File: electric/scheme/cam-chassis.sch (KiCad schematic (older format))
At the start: 45 parts, among them IC1 ATMEGA8-AI, K1 pyro, P1 TST, P2 TST, P3 TST, P4 TST, P5 TST, P6 TST, P7 servo, Q3 bc857, Q4 bc847, Q5 irlml2244, Q6 NPN, Q7 irlml2244, U1 MINI-USB-B-4-bases, Y1 Crystal

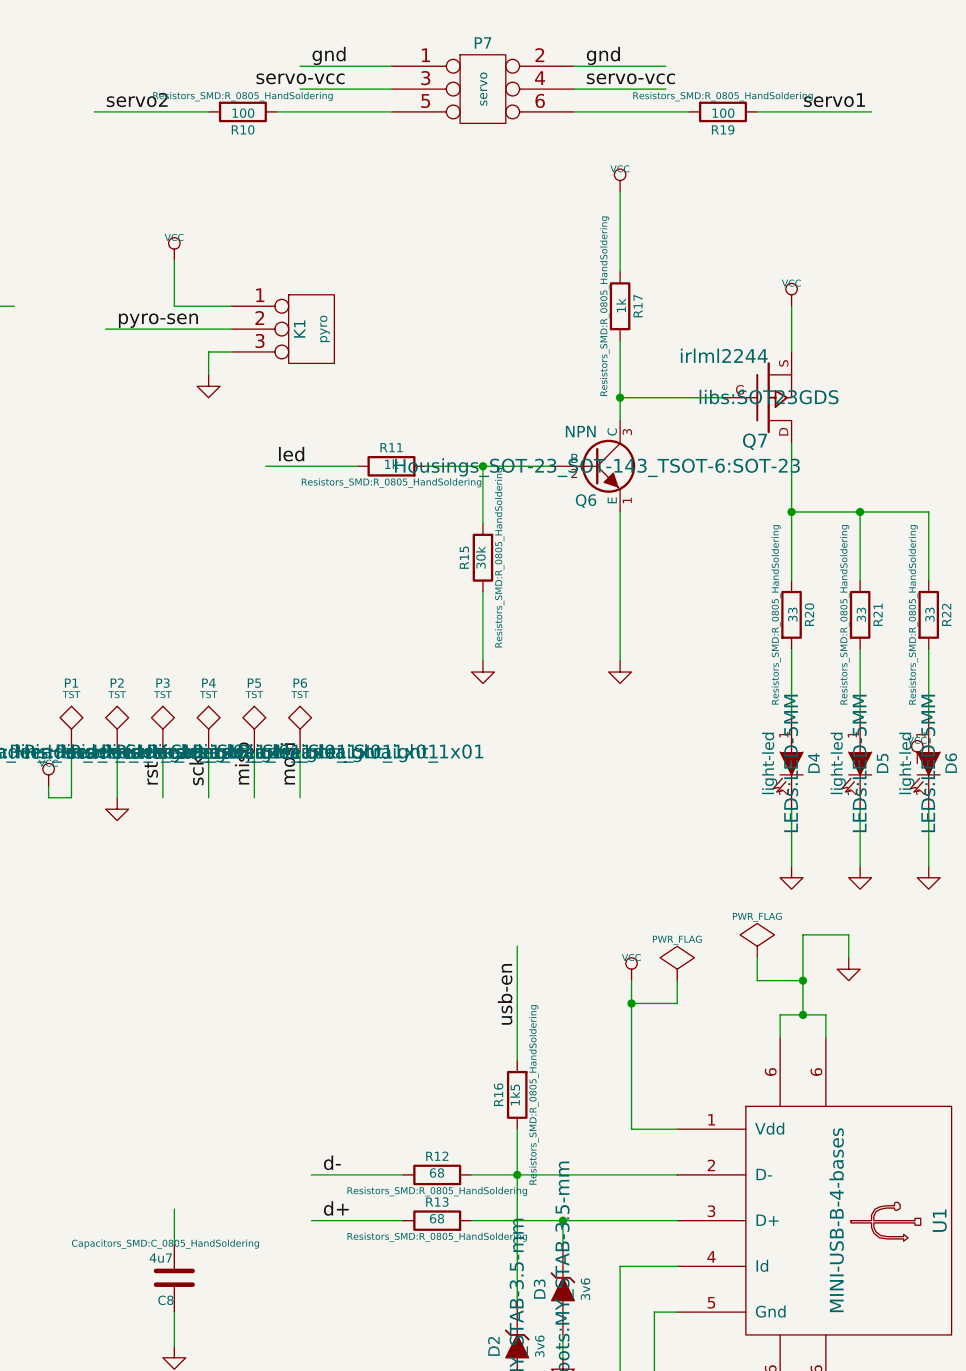
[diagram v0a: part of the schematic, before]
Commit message: Made LEDs power also limited.
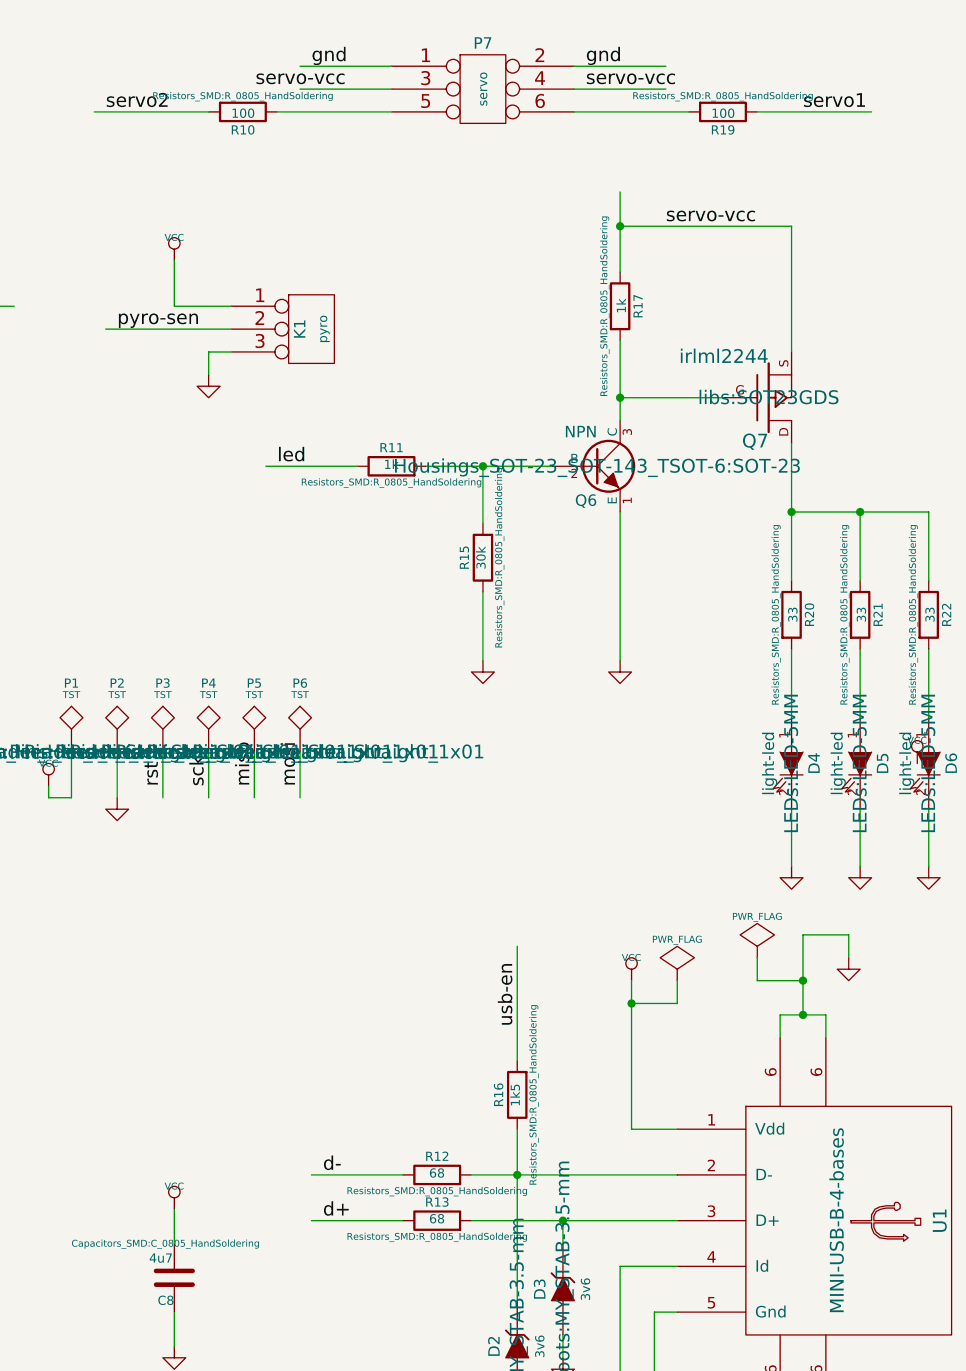
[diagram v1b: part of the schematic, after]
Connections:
- wire segments 138 -> 139
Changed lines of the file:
@@
 NoConn ~ 6000 1350
 $Comp
-L VCC #PWR032
-U 1 1 55300EC2
-P 9600 1450
-F 0 "#PWR032" H 9600 1550 30  0001 C CNN
-F 1 "VCC" H 9600 1550 30  0000 C CNN
-F 2 "" H 9600 1450 60  0000 C CNN
-F 3 "" H 9600 1450 60  0000 C CNN
-	1    9600 1450
-	1    0    0    -1
-$EndComp
-$Comp
-L VCC #PWR033
-U 1 1 55300EC8
-P 10350 1950
-F 0 "#PWR033" H 10350 2050 30  0001 C CNN
-F 1 "VCC" H 10350 2050 30  0000 C CNN
-F 2 "" H 10350 1950 60  0000 C CNN
-F 3 "" H 10350 1950 60  0000 C CNN
-	1    10350 1950
-	1    0    0    -1
-$EndComp
-$Comp
-L PWR_FLAG #FLG034
+L PWR_FLAG #FLG032
 U 1 1 552FFAA1
 P 9850 4900
-F 0 "#FLG034" H 9850 4995 30  0001 C CNN
+F 0 "#FLG032" H 9850 4995 30  0001 C CNN
 F 1 "PWR_FLAG" H 9850 5080 30  0000 C CNN
 F 2 "" H 9850 4900 60  0000 C CNN
@@
 Connection ~ 10650 2850
 Wire Wire Line
-	10350 2150 10350 1950
+	10350 1600 10350 2150
 Wire Wire Line
 	10050 2350 9600 2350
@@
 	0    -1   1    0
 $EndComp
+Text Label 9800 1600 0    60   ~ 0
+servo-vcc
+Wire Wire Line
+	9600 1600 10350 1600
+Connection ~ 9600 1600
+$Comp
+L VCC #PWR033
+U 1 1 55B85E1E
+P 7650 5900
+F 0 "#PWR033" H 7650 6000 30  0001 C CNN
+F 1 "VCC" H 7650 6000 30  0000 C CNN
+F 2 "" H 7650 5900 60  0000 C CNN
+F 3 "" H 7650 5900 60  0000 C CNN
+	1    7650 5900
+	1    0    0    -1
+$EndComp
 $EndSCHEMATC

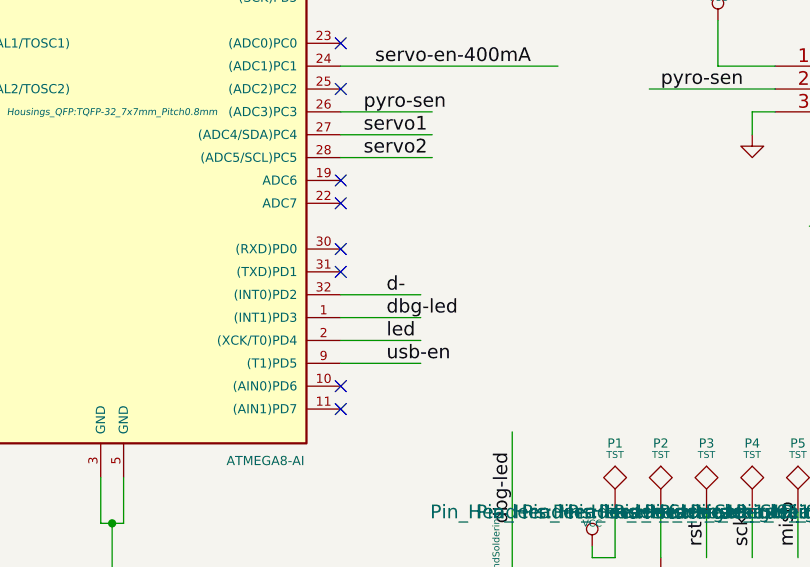
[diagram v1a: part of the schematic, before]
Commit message: INT0 must be connected to D+ - not D- (!!!)
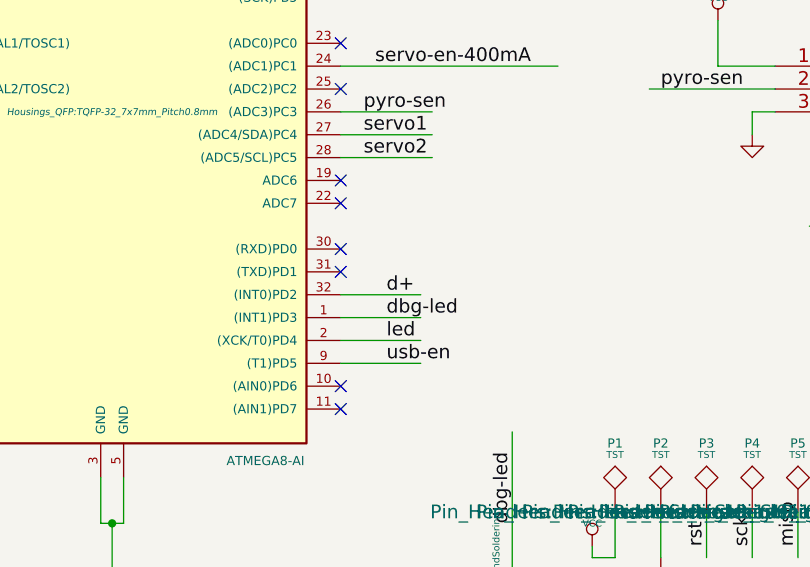
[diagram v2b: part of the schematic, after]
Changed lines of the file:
@@
 $EndComp
 Text Label 6200 2950 0    60   ~ 0
-d-
+d+
 Text Label 6450 1250 0    60   ~ 0
 d+
